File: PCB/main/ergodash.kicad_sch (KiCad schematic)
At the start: 97 parts, among them J1 Conn_01x04, J2 Conn_01x15, SW1 SW_PUSH, SW10 SW_PUSH, SW11 SW_PUSH, SW12 SW_PUSH, SW13 SW_PUSH, SW14 SW_PUSH, SW15 SW_PUSH, SW16 SW_PUSH, SW17 SW_PUSH, SW18 SW_PUSH, SW19 SW_PUSH, SW2 SW_PUSH, SW20 SW_PUSH, SW21 SW_PUSH, SW22 SW_PUSH, SW23 SW_PUSH, SW24 SW_PUSH, SW25 SW_PUSH, SW26 SW_PUSH, SW27 SW_PUSH, SW28 SW_PUSH, SW3 SW_PUSH, SW30 SW_PUSH, SW31 SW_PUSH, SW32 SW_PUSH, SW33 SW_PUSH, SW34 SW_PUSH, SW35 SW_PUSH, SW36 SW_PUSH, SW38 SW_PUSH, SW39 SW_PUSH, SW4 SW_PUSH, SW40 SW_PUSH, SW41 SW_PUSH, SW5 SW_PUSH, SW6 SW_PUSH, SW7 SW_PUSH, SW8 SW_PUSH, SW9 SW_PUSH

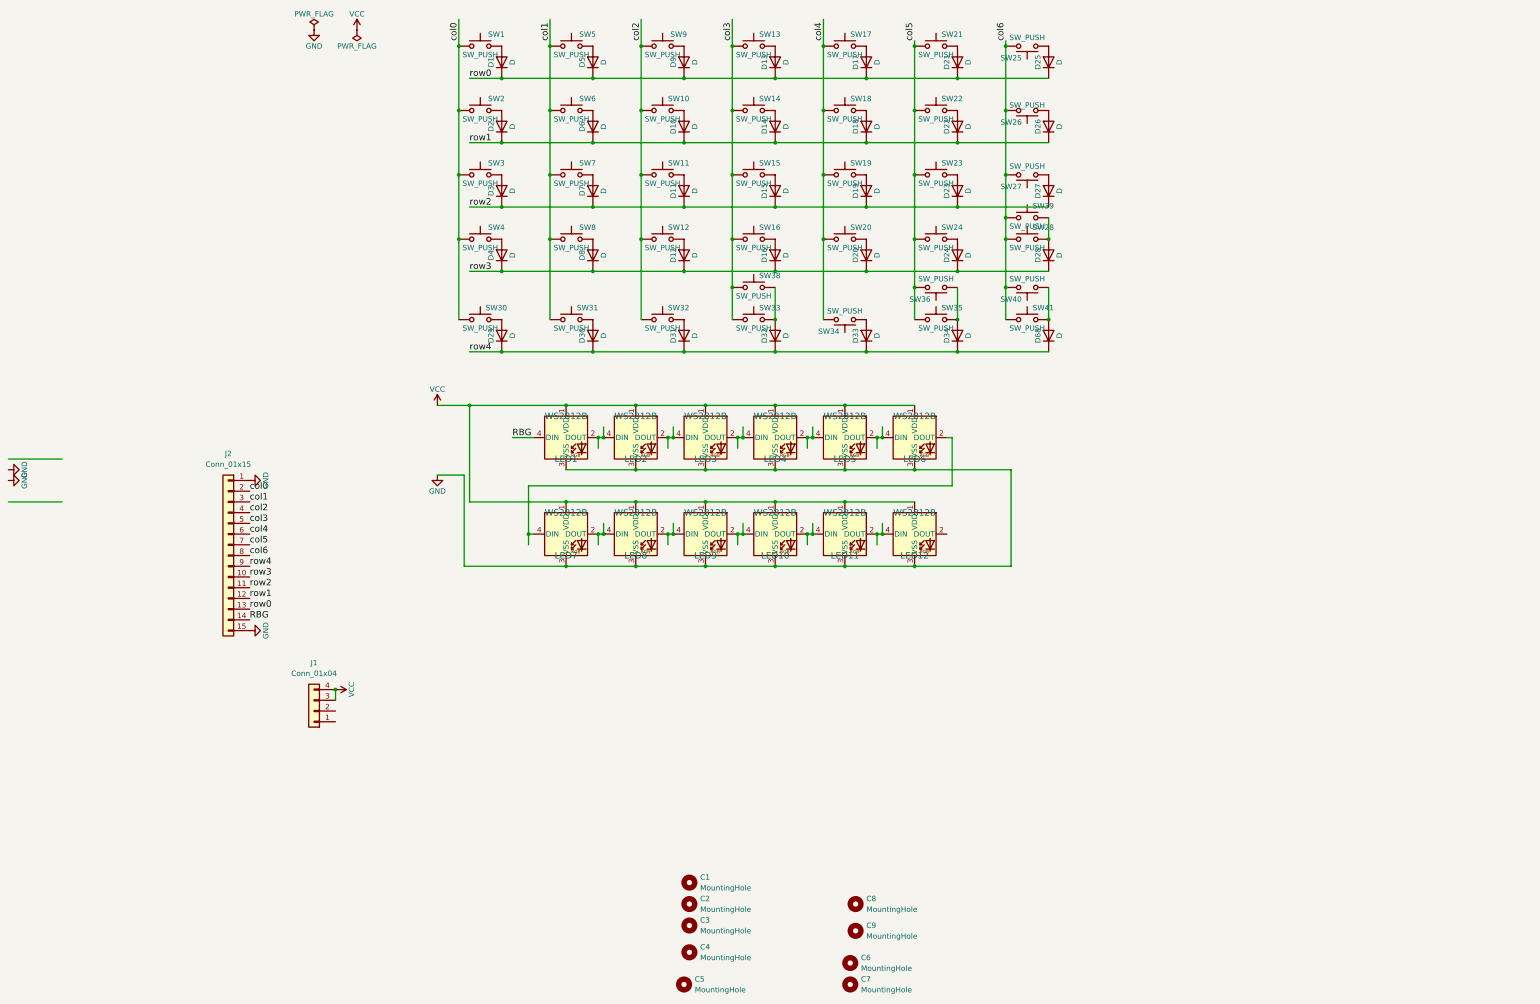
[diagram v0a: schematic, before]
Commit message: without led
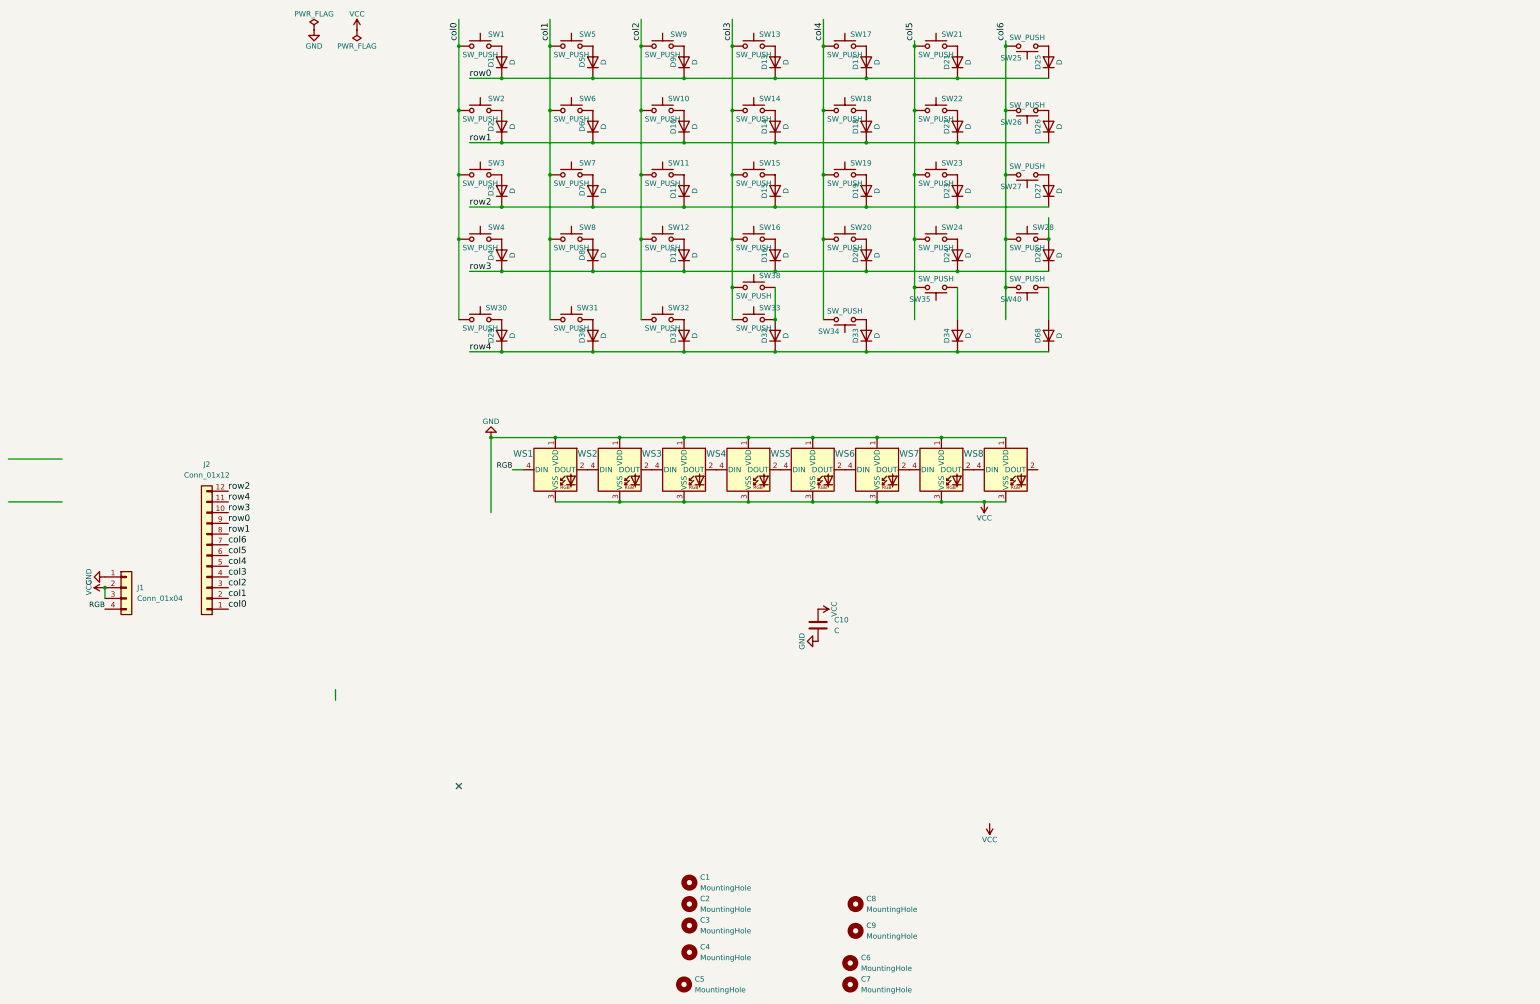
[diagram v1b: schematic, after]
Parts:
- removed J2: Conn_01x15, Connector_FFC-FPC:Molex_502244-1530_1x15-1MP_P0.5mm_Horizontal, symbol Connector_Generic:Conn_01x15
- removed LED1, LED10, LED11, LED12, LED2, LED3, LED4, LED5, LED6, LED7, LED8, LED9: WS2812B, ergodash_2040:WS2812B-5, symbol LED:WS2812B
- removed SW35, SW39, SW41: SW_PUSH, ergodash_2040:Kailh_socket_MX, symbol Switch:SW_Push
- added C10: C, Capacitor_SMD:C_1206_3216Metric, symbol Device:C
- added J2: Conn_01x12, ergodash_2040:HDGC_1.0K-J-12PW, symbol Connector_Generic:Conn_01x12
- added WS1, WS2, WS3, WS4, WS5, WS6, WS7, WS8: WS2812B, ergodash_2040:LED_WS2812B_reversible, symbol LED:WS2812B
- D1, D10, D11, D12, D13, D14, D15, D16, D17, D18, D19, D2, D20, D21, D22, D23, D24, D25, D26, D27, D28, D29, D3, D30, D31, D32, D33, D34, D4, D5, D6, D68, D7, D8, D9: footprint ergodash_2040:Diode_SMD_reversible -> ergodash_2040:D_SOD-123-dobuleside
- J1: footprint (none) -> Connector_JST:JST_SH_SM04B-SRSS-TB_1x04-1MP_P1.00mm_Horizontal
- SW28: footprint ergodash_2040:Kailh_socket_MX_rightmost -> ergodash_2040:Kailh_socket_MX
- renumbered SW36 to SW35
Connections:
- net GND: now also J1.1 (Pin_1), C10.2, WS1.1 (VDD), WS2.1 (VDD), WS3.1 (VDD), WS4.1 (VDD), WS5.1 (VDD), WS6.1 (VDD), WS7.1 (VDD), WS8.1 (VDD)
- net VCC: now also J1.2 (Pin_2), C10.1, WS1.3 (VSS), WS2.3 (VSS), WS3.3 (VSS), WS4.3 (VSS), WS5.3 (VSS), WS6.3 (VSS), WS7.3 (VSS), WS8.3 (VSS); no longer J1.4 (Pin_4)
- net col0: now also J2.1 (Pin_1)
- net col1: now also J2.2 (Pin_2)
- net col2: now also J2.3 (Pin_3)
- net col3: now also J2.4 (Pin_4)
- net col4: now also J2.5 (Pin_5)
- net col5: now also J2.6 (Pin_6)
- net col6: now also J2.7 (Pin_7)
- net row0: now also J2.9 (Pin_9)
- net row1: now also J2.8 (Pin_8)
- net row2: now also J2.12 (Pin_12)
- net row3: now also J2.10 (Pin_10)
- net row4: now also J2.11 (Pin_11)
- new net: WS4.2 (DOUT), WS5.4 (DIN)
- new net: WS3.2 (DOUT), WS4.4 (DIN)
- new net: WS7.2 (DOUT), WS8.4 (DIN)
- new net: WS6.2 (DOUT), WS7.4 (DIN)
- new net: WS2.2 (DOUT), WS3.4 (DIN)
- new net: WS1.2 (DOUT), WS2.4 (DIN)
- new net: WS5.2 (DOUT), WS6.4 (DIN)
- new net RGB: J1.4 (Pin_4), WS1.4 (DIN)
- no-connect marks 0 -> 1

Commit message: before cut
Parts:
- removed SW33: SW_PUSH, ergodash_2040:Kailh_socket_MX, symbol Switch:SW_Push
- added LED1, LED10, LED11, LED12, LED13, LED14, LED15, LED16, LED17, LED18, LED19, LED2, LED20, LED21, LED22, LED24, LED29, LED3, LED30, LED31, LED33, LED34, LED35, LED36, LED4, LED5, LED6, LED7, LED8, LED9: LED, ergodash_2040:LED_MX_3mm, symbol Device:LED
- added LED23, LED25, LED26, LED27, LED28: LED, ergodash_2040:LED_MX_3mm_flip, symbol Device:LED
- added Q1: BSS138, Package_TO_SOT_SMD:SOT-23, symbol Transistor_FET:BSS138
- added R1: 1k, Resistor_SMD:R_1206_3216Metric_Pad1.30x1.75mm_HandSolder, symbol Device:R
- added WS9: WS2812B, ergodash_2040:LED_WS2812B_reversible, symbol LED:WS2812B
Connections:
- net GND: now also Q1.2 (S), WS9.1 (VDD)
- net at WS3.4 (DIN): now also WS9.2 (DOUT); no longer WS2.2 (DOUT)
- net VCC renamed +5V
- net +5V: now also LED1.2 (A), LED10.2 (A), LED11.2 (A), LED12.2 (A), LED13.2 (A), LED14.2 (A), LED15.2 (A), LED16.2 (A), LED17.2 (A), LED18.2 (A), LED19.2 (A), LED2.2 (A), LED20.2 (A), LED21.2 (A), LED22.2 (A), LED23.2 (A), LED24.2 (A), LED25.2 (A), LED26.2 (A), LED27.2 (A), LED28.2 (A), LED29.2 (A), LED3.2 (A), LED30.2 (A), LED31.2 (A), LED33.2 (A), LED34.2 (A), LED35.2 (A), LED36.2 (A), LED4.2 (A), LED5.2 (A), LED6.2 (A), LED7.2 (A), LED8.2 (A), LED9.2 (A), WS9.3 (VSS); no longer J1.3 (Pin_3)
- new net: WS2.2 (DOUT), WS9.4 (DIN)
- new net: Q1.1 (G), R1.2
- new net Backlight: J1.3 (Pin_3), R1.1
- new net leds: LED1.1 (K), LED10.1 (K), LED11.1 (K), LED12.1 (K), LED13.1 (K), LED14.1 (K), LED15.1 (K), LED16.1 (K), LED17.1 (K), LED18.1 (K), LED19.1 (K), LED2.1 (K), LED20.1 (K), LED21.1 (K), LED22.1 (K), LED23.1 (K), LED24.1 (K), LED25.1 (K), LED26.1 (K), LED27.1 (K), LED28.1 (K), LED29.1 (K), LED3.1 (K), LED30.1 (K), LED31.1 (K), LED33.1 (K), LED34.1 (K), LED35.1 (K), LED36.1 (K), LED4.1 (K), LED5.1 (K), LED6.1 (K), LED7.1 (K), LED8.1 (K), LED9.1 (K), Q1.3 (D)
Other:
- moved on the sheet: C10, WS3, WS4, WS5, WS6, WS7, WS8

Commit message: simpler version
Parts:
- removed C1, C2, C3, C4, C5, C6, C7, C8, C9: MountingHole, ergodash_2040:Plate_MountingHole_cut, symbol Mechanical:MountingHole
- removed LED1, LED10, LED11, LED12, LED13, LED14, LED15, LED16, LED17, LED18, LED19, LED2, LED20, LED21, LED22, LED24, LED29, LED3, LED30, LED31, LED33, LED34, LED35, LED36, LED4, LED5, LED6, LED7, LED8, LED9: LED, ergodash_2040:LED_MX_3mm, symbol Device:LED
- removed LED23, LED25, LED26, LED27, LED28: LED, ergodash_2040:LED_MX_3mm_flip, symbol Device:LED
- removed Q1: BSS138, Package_TO_SOT_SMD:SOT-23, symbol Transistor_FET:BSS138
- removed R1: 1k, Resistor_SMD:R_1206_3216Metric_Pad1.30x1.75mm_HandSolder, symbol Device:R
- added H1, H2, H3, H4, H5, H6: MountingHole, ergodash_2040:MountingHole_5mm, symbol Mechanical:MountingHole
- C10: footprint Capacitor_SMD:C_1206_3216Metric -> ergodash_2040:C_1206_3216Metric
- D1, D10, D11, D12, D13, D14, D15, D16, D17, D18, D19, D2, D20, D21, D22, D23, D24, D25, D26, D27, D28, D29, D3, D30, D31, D33, D4, D5, D6, D7, D8, D9: footprint ergodash_2040:D_SOD-123-dobuleside -> ergodash_2040:Diode_SMD_reversible
- D35: renamed from D34; footprint ergodash_2040:D_SOD-123-dobuleside -> ergodash_2040:Diode_SMD_reversible
- D38: renamed from D32; footprint ergodash_2040:D_SOD-123-dobuleside -> ergodash_2040:Diode_SMD_reversible
- D40: renamed from D68; footprint ergodash_2040:D_SOD-123-dobuleside -> ergodash_2040:Diode_SMD_reversible
- J1: footprint Connector_JST:JST_SH_SM04B-SRSS-TB_1x04-1MP_P1.00mm_Horizontal -> ergodash_2040:JST_SH_SM04B-SRSS-TB_1x04-1MP_P1.00mm_Horizontal
- SW40: footprint ergodash_2040:Kailh_socket_MX -> ergodash_2040:Kailh_socket_MX_2u
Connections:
- net Backlight is gone; now on net +5V: J1.3 (Pin_3)
- net +5V: now also WS1.1 (VDD), WS2.1 (VDD), WS3.1 (VDD), WS4.1 (VDD), WS5.1 (VDD), WS6.1 (VDD), WS7.1 (VDD), WS8.1 (VDD), WS9.1 (VDD); no longer WS1.3 (VSS), WS2.3 (VSS), WS3.3 (VSS), WS4.3 (VSS), WS5.3 (VSS), WS6.3 (VSS), WS7.3 (VSS), WS8.3 (VSS), WS9.3 (VSS)
- net GND: now also WS1.3 (VSS), WS2.3 (VSS), WS3.3 (VSS), WS4.3 (VSS), WS5.3 (VSS), WS6.3 (VSS), WS7.3 (VSS), WS8.3 (VSS), WS9.3 (VSS); no longer WS1.1 (VDD), WS2.1 (VDD), WS3.1 (VDD), WS4.1 (VDD), WS5.1 (VDD), WS6.1 (VDD), WS7.1 (VDD), WS8.1 (VDD), WS9.1 (VDD)
- net row0: now also J2.8 (Pin_8); no longer J2.9 (Pin_9)
- net row1: now also J2.9 (Pin_9); no longer J2.8 (Pin_8)
